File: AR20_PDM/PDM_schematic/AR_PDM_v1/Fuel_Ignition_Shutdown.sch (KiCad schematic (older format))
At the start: 21 parts

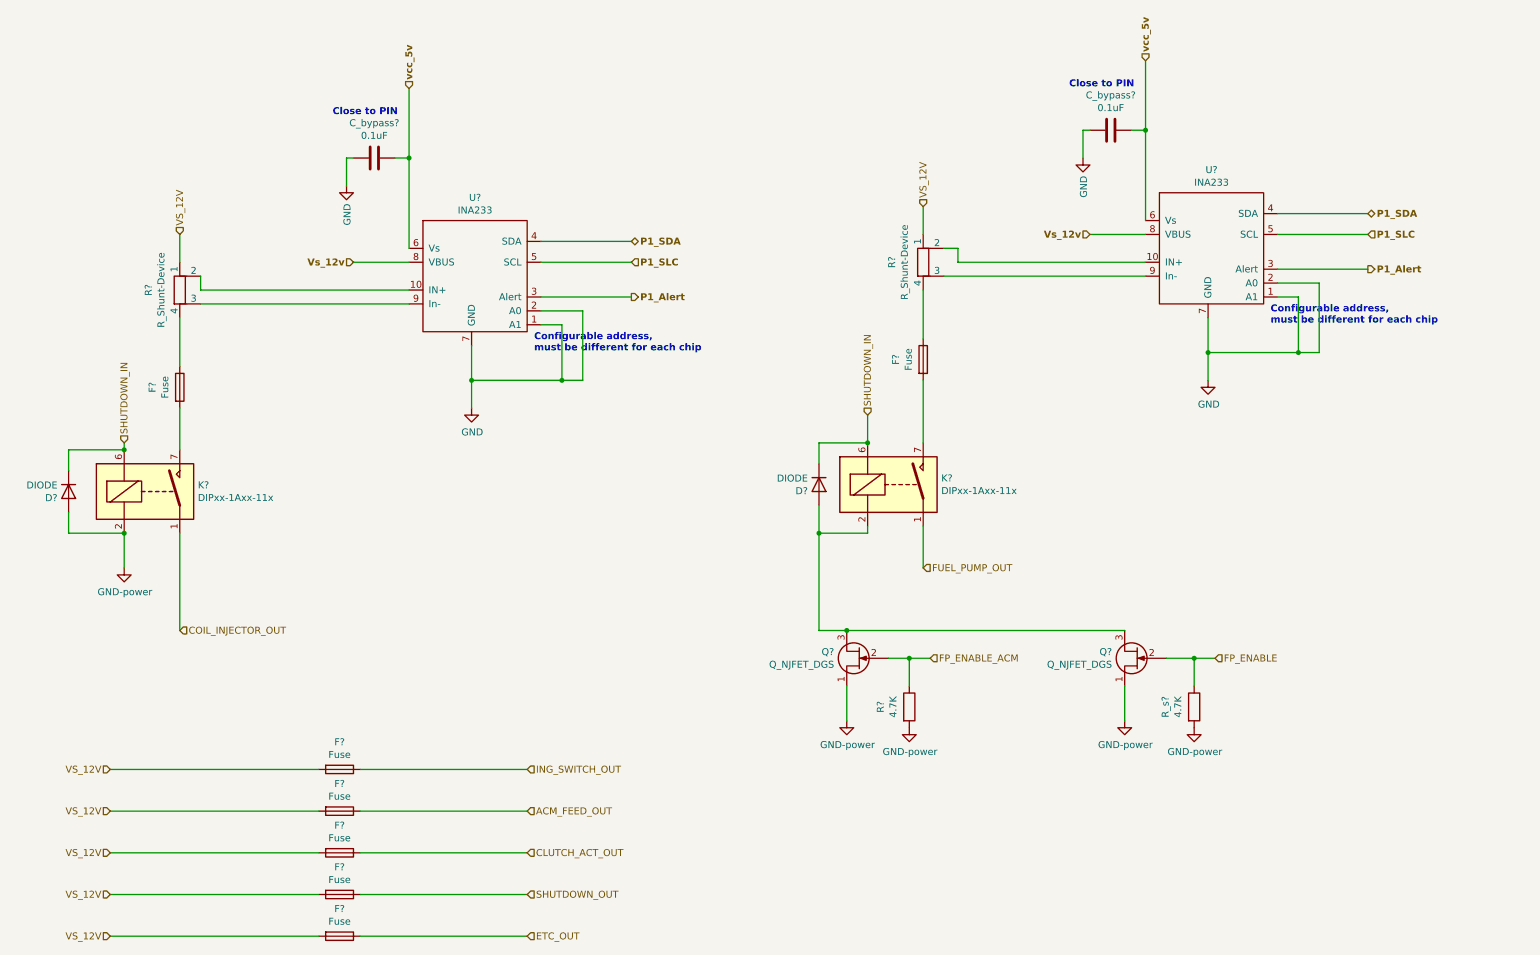
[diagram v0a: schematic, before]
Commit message: First draft of Gear phase, shutdown relays, and Direct phases.
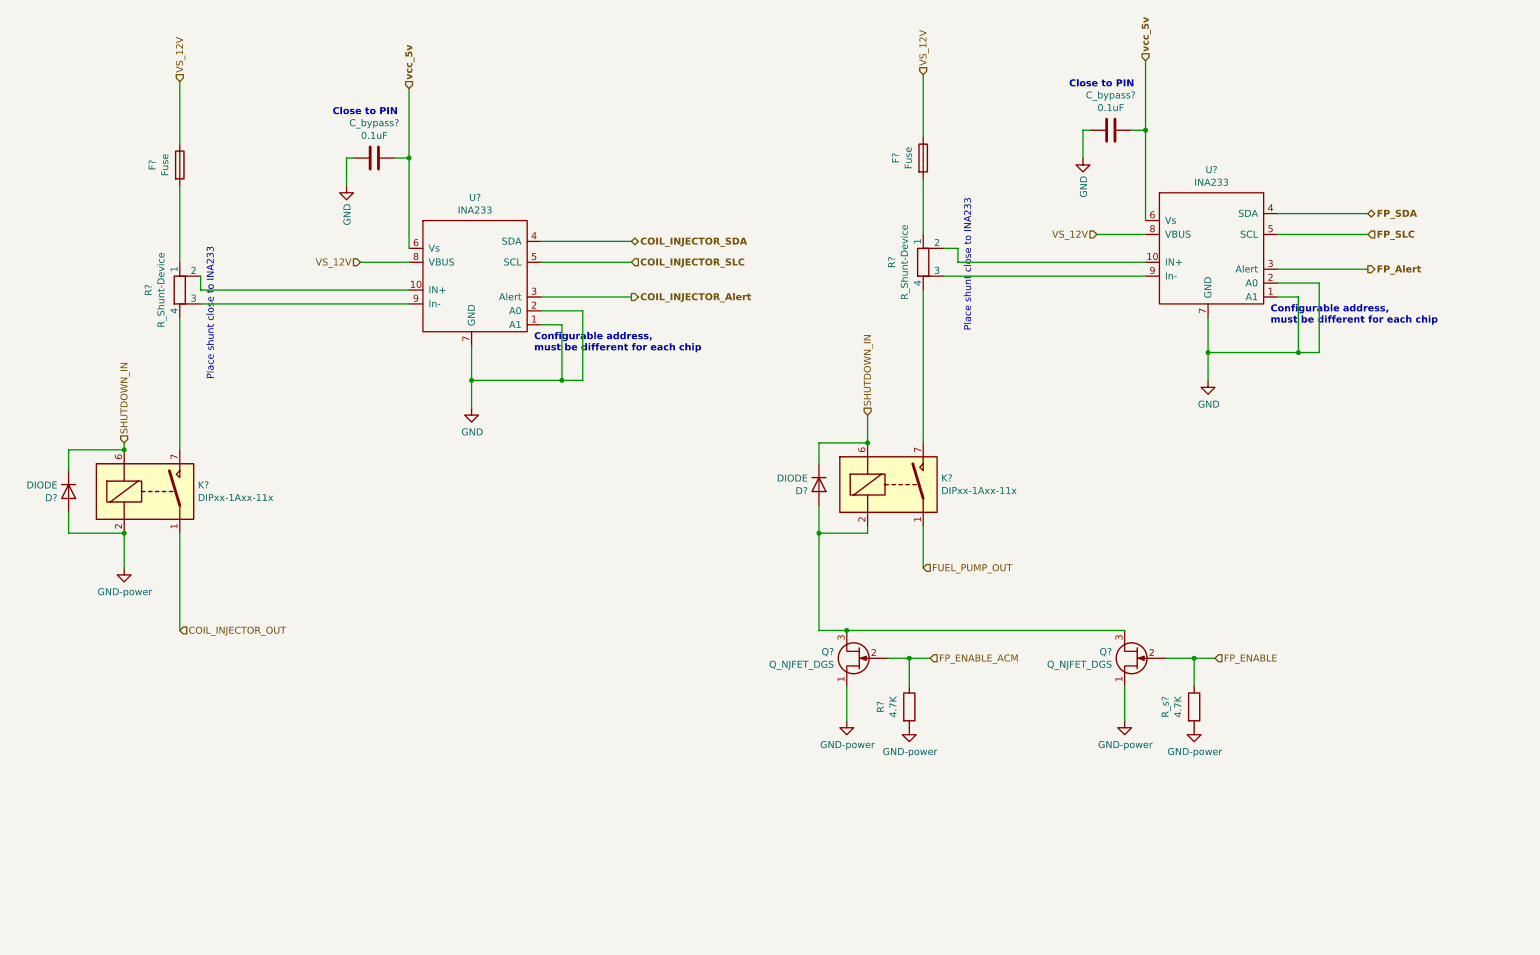
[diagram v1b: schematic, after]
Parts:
- removed F? (x6): Fuse, symbol Device:Fuse
- added F?: Fuse, symbol Device:Fuse
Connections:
- net Vs_12v is gone; now on net VS_12V: U?.8 (VBUS), U?.8 (VBUS)
- net VS_12V: now also F?.1, F?.1; no longer R?.1, R?.1
- net at R?.4: now also K?.7, K?.8
- net at K?.7, K?.8: now also R?.4; no longer F?.2
- net P1_Alert renamed COIL_INJECTOR_Alert
- net COIL_INJECTOR_Alert: no longer U?.3 (Alert)
- net P1_SDA renamed COIL_INJECTOR_SDA
- net COIL_INJECTOR_SDA: no longer U?.4 (SDA)
- net P1_SLC renamed COIL_INJECTOR_SLC
- net COIL_INJECTOR_SLC: no longer U?.5 (SCL)
- new net: F?.2, R?.1 (x2)
- new net FP_Alert: U?.3 (Alert)
- new net FP_SDA: U?.4 (SDA)
- new net FP_SLC: U?.5 (SCL)
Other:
- note added: "Place shunt close to INA233\n"
- moved on the sheet: F?
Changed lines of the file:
@@
 $Descr A4 11693 8268
 encoding utf-8
-Sheet 2 4
+Sheet 5 6
 Title ""
 Date ""
@@
 Comment4 ""
 $EndDescr
-$Comp
-L Device:Fuse F?
-U 1 1 5DDB2D60
-P 3150 6000
-F 0 "F?" V 2953 6000 50  0000 C CNN
-F 1 "Fuse" V 3044 6000 50  0000 C CNN
-F 2 "" V 3080 6000 50  0001 C CNN
-F 3 "~" H 3150 6000 50  0001 C CNN
-	1    3150 6000
-	0    1    1    0
-$EndComp
-Wire Wire Line
-	3000 6000 1500 6000
-Wire Wire Line
-	3300 6000 4500 6000
-Text HLabel 1500 6000 0    50   Input ~ 0
-VS_12V
-$Comp
-L Device:Fuse F?
-U 1 1 5DDB4A05
-P 3150 6300
-F 0 "F?" V 2953 6300 50  0000 C CNN
-F 1 "Fuse" V 3044 6300 50  0000 C CNN
-F 2 "" V 3080 6300 50  0001 C CNN
-F 3 "~" H 3150 6300 50  0001 C CNN
-	1    3150 6300
-	0    1    1    0
-$EndComp
-Wire Wire Line
-	3000 6300 1500 6300
-Wire Wire Line
-	3300 6300 4500 6300
-Text HLabel 1500 6300 0    50   Input ~ 0
-VS_12V
-$Comp
-L Device:Fuse F?
-U 1 1 5DDB4CFC
-P 3150 6600
-F 0 "F?" V 2953 6600 50  0000 C CNN
-F 1 "Fuse" V 3044 6600 50  0000 C CNN
-F 2 "" V 3080 6600 50  0001 C CNN
-F 3 "~" H 3150 6600 50  0001 C CNN
-	1    3150 6600
-	0    1    1    0
-$EndComp
-Wire Wire Line
-	3000 6600 1500 6600
-Wire Wire Line
-	3300 6600 4500 6600
-Text HLabel 1500 6600 0    50   Input ~ 0
-VS_12V
-$Comp
-L Device:Fuse F?
-U 1 1 5DDB67ED
-P 3150 6900
-F 0 "F?" V 2953 6900 50  0000 C CNN
-F 1 "Fuse" V 3044 6900 50  0000 C CNN
-F 2 "" V 3080 6900 50  0001 C CNN
-F 3 "~" H 3150 6900 50  0001 C CNN
-	1    3150 6900
-	0    1    1    0
-$EndComp
-Wire Wire Line
-	3000 6900 1500 6900
-Wire Wire Line
-	3300 6900 4500 6900
-Text HLabel 1500 6900 0    50   Input ~ 0
-VS_12V
-$Comp
-L Device:Fuse F?
-U 1 1 5DDB67F6
-P 3150 7200
-F 0 "F?" V 2953 7200 50  0000 C CNN
-F 1 "Fuse" V 3044 7200 50  0000 C CNN
-F 2 "" V 3080 7200 50  0001 C CNN
-F 3 "~" H 3150 7200 50  0001 C CNN
-	1    3150 7200
-	0    1    1    0
-$EndComp
-Wire Wire Line
-	3000 7200 1500 7200
-Wire Wire Line
-	3300 7200 4500 7200
-Text HLabel 1500 7200 0    50   Input ~ 0
-VS_12V
-Text HLabel 4500 6000 2    50   Input ~ 0
-ING_SWITCH_OUT
-Text HLabel 4500 6300 2    50   Input ~ 0
-ACM_FEED_OUT
-Text HLabel 4500 6600 2    50   Input ~ 0
-CLUTCH_ACT_OUT
-Text HLabel 4500 6900 2    50   Input ~ 0
-SHUTDOWN_OUT
-Text HLabel 4500 7200 2    50   Input ~ 0
-ETC_OUT
 Text HLabel 7350 4550 2    50   Input ~ 0
 FUEL_PUMP_OUT
@@
 	1    0    0    -1
 $EndComp
-Text HLabel 7350 1950 1    50   Input ~ 0
+Text HLabel 7350 1000 1    50   Input ~ 0
 VS_12V
 $Comp
 L Device:Fuse F?
 U 1 1 5DDF15AA
-P 7350 3050
-F 0 "F?" V 7153 3050 50  0000 C CNN
-F 1 "Fuse" V 7244 3050 50  0000 C CNN
-F 2 "" V 7280 3050 50  0001 C CNN
-F 3 "~" H 7350 3050 50  0001 C CNN
-	1    7350 3050
-	1    0    0    -1
-$EndComp
-Wire Wire Line
-	7350 1950 7350 2150
-Wire Wire Line
-	7350 2550 7350 2900
-Wire Wire Line
-	7350 3200 7350 3650
+P 7350 1600
+F 0 "F?" V 7153 1600 50  0000 C CNN
+F 1 "Fuse" V 7244 1600 50  0000 C CNN
+F 2 "" V 7280 1600 50  0001 C CNN
+F 3 "~" H 7350 1600 50  0001 C CNN
+	1    7350 1600
+	1    0    0    -1
+$EndComp
 $Comp
 L AR20_PDM_v1-rescue:C-Device C_bypass?
 U 1 1 5DE0EACB
 P 8700 1400
+AR Path="/5DA89415/5DE0EACB" Ref="C_bypass?"  Part="1"
+AR Path="/5DA8920B/5DE0EACB" Ref="C_bypass?"  Part="1"
 F 0 "C_bypass?" V 8448 1400 50  0000 C CNN
 F 1 "0.1uF" V 8539 1400 50  0000 C CNN
@@
 U 1 1 5DE0EAD1
 P 8500 1600
+AR Path="/5DA89415/5DE0EAD1" Ref="#PWR?"  Part="1"
+AR Path="/5DA8920B/5DE0EAD1" Ref="#PWR?"  Part="1"
 F 0 "#PWR?" H 8500 1350 50  0001 C CNN
 F 1 "GND" V 8505 1472 50  0000 R CNN
@@
 U 1 1 5DE0EAD8
 P 9400 3200
+AR Path="/5DA89415/5DE0EAD8" Ref="#PWR?"  Part="1"
+AR Path="/5DA8920B/5DE0EAD8" Ref="#PWR?"  Part="1"
 F 0 "#PWR?" H 9400 2950 50  0001 C CNN
 F 1 "GND" H 9405 3027 50  0000 C CNN
@@
 U 1 1 5DE0EAE7
 P 9400 2100
+AR Path="/5DA89415/5DE0EAE7" Ref="U?"  Part="1"
+AR Path="/5DA8920B/5DE0EAE7" Ref="U?"  Part="1"
 F 0 "U?" H 9425 2515 50  0000 C CNN
 F 1 "INA233" H 9425 2424 50  0000 C CNN
@@
 	1    0    0    -1
 $EndComp
-Text HLabel 8550 2150 0    50   Input ~ 10
-Vs_12v
 Text HLabel 8950 900  1    50   Input ~ 10
 vcc_5v
 Text HLabel 10550 2400 2    50   Output ~ 10
-P1_Alert
+FP_Alert
 Text HLabel 10550 2000 2    50   BiDi ~ 10
-P1_SDA
+FP_SDA
 Text HLabel 10550 2150 2    50   Input ~ 10
-P1_SLC
+FP_SLC
 Text Notes 8400 1100 0    50   ~ 10
 Close to PIN
-Wire Wire Line
-	8950 2150 8550 2150
 Wire Wire Line
 	9900 2150 10550 2150
@@
 Wire Wire Line
 	4600 2350 5250 2350
-Wire Wire Line
-	3650 2350 3250 2350
 Text Notes 3100 1300 0    50   ~ 10
 Close to PIN
 Text HLabel 5250 2350 2    50   Input ~ 10
-P1_SLC
+COIL_INJECTOR_SLC
 Text HLabel 5250 2200 2    50   BiDi ~ 10
-P1_SDA
+COIL_INJECTOR_SDA
 Text HLabel 5250 2600 2    50   Output ~ 10
-P1_Alert
+COIL_INJECTOR_Alert
 Text HLabel 3650 1100 1    50   Input ~ 10
 vcc_5v
-Text HLabel 3250 2350 0    50   Input ~ 10
-Vs_12v
 $Comp
 L AR20_PDM_v1-rescue:INA233 U?
 U 1 1 5DE077D0
 P 4100 2300
+AR Path="/5DA89415/5DE077D0" Ref="U?"  Part="1"
+AR Path="/5DA8920B/5DE077D0" Ref="U?"  Part="1"
 F 0 "U?" H 4125 2715 50  0000 C CNN
 F 1 "INA233" H 4125 2624 50  0000 C CNN
@@
 U 1 1 5DE077C1
 P 4100 3400
+AR Path="/5DA89415/5DE077C1" Ref="#PWR?"  Part="1"
+AR Path="/5DA8920B/5DE077C1" Ref="#PWR?"  Part="1"
 F 0 "#PWR?" H 4100 3150 50  0001 C CNN
 F 1 "GND" H 4105 3227 50  0000 C CNN
@@
 U 1 1 5DE077BA
 P 3200 1800
+AR Path="/5DA89415/5DE077BA" Ref="#PWR?"  Part="1"
+AR Path="/5DA8920B/5DE077BA" Ref="#PWR?"  Part="1"
 F 0 "#PWR?" H 3200 1550 50  0001 C CNN
 F 1 "GND" V 3205 1672 50  0000 R CNN
@@
 U 1 1 5DE077B4
 P 3400 1600
+AR Path="/5DA89415/5DE077B4" Ref="C_bypass?"  Part="1"
+AR Path="/5DA8920B/5DE077B4" Ref="C_bypass?"  Part="1"
 F 0 "C_bypass?" V 3148 1600 50  0000 C CNN
 F 1 "0.1uF" V 3239 1600 50  0000 C CNN
@@
 	0    1    1    0
 $EndComp
-Wire Wire Line
-	2000 2750 2000 3100
-Wire Wire Line
-	2000 2150 2000 2350
-$Comp
-L Device:Fuse F?
-U 1 1 5DDB7458
-P 2000 3250
-F 0 "F?" V 1803 3250 50  0000 C CNN
-F 1 "Fuse" V 1894 3250 50  0000 C CNN
-F 2 "" V 1930 3250 50  0001 C CNN
-F 3 "~" H 2000 3250 50  0001 C CNN
-	1    2000 3250
-	1    0    0    -1
-$EndComp
-Text HLabel 2000 2150 1    50   Input ~ 0
-VS_12V
 $Comp
 L Relay:DIPxx-1Axx-11x K?
@@
 Text HLabel 1600 3650 1    50   Input ~ 0
 SHUTDOWN_IN
-Wire Wire Line
-	2000 3400 2000 3700
 Wire Wire Line
 	1600 3700 1200 3700
@@
 	1    0    0    -1
 $EndComp
+Wire Wire Line
+	7350 1450 7350 1000
+Text HLabel 2000 1050 1    50   Input ~ 0
+VS_12V
+$Comp
+L Device:Fuse F?
+U 1 1 5DE5EBA7
+P 2000 1650
+F 0 "F?" V 1803 1650 50  0000 C CNN
+F 1 "Fuse" V 1894 1650 50  0000 C CNN
+F 2 "" V 1930 1650 50  0001 C CNN
+F 3 "~" H 2000 1650 50  0001 C CNN
+	1    2000 1650
+	1    0    0    -1
+$EndComp
+Wire Wire Line
+	2000 1500 2000 1050
+Wire Wire Line
+	2000 2750 2000 3700
+Wire Wire Line
+	7350 2550 7350 3650
+Text Notes 2250 3200 1    50   ~ 0
+Place shunt close to INA233\n
+Text Notes 7700 2850 1    50   ~ 0
+Place shunt close to INA233\n
+Wire Wire Line
+	2000 1800 2000 2350
+Text HLabel 3300 2350 0    50   Input ~ 0
+VS_12V
+Wire Wire Line
+	3650 2350 3300 2350
+Wire Wire Line
+	7350 1750 7350 2150
+Text HLabel 8600 2150 0    50   Input ~ 0
+VS_12V
+Wire Wire Line
+	8600 2150 8950 2150
 $EndSCHEMATC

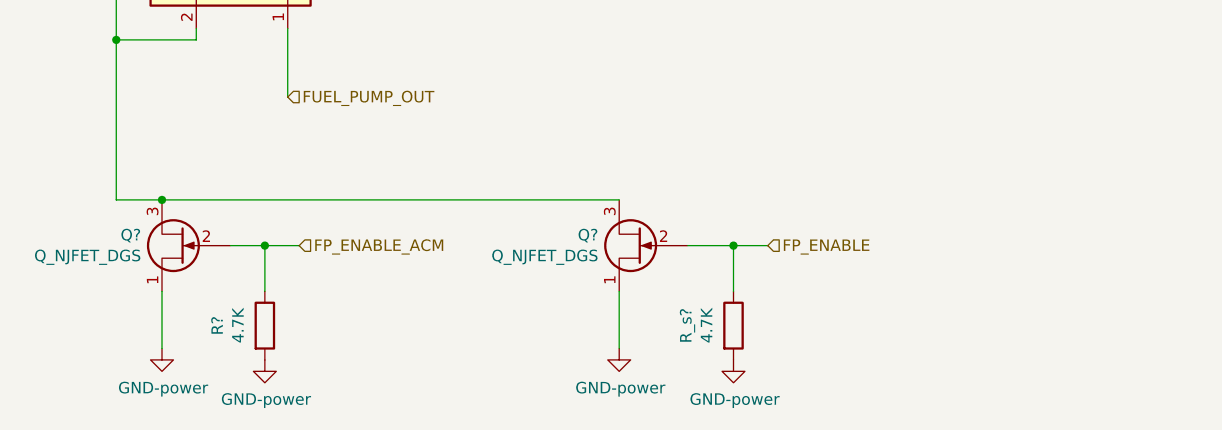
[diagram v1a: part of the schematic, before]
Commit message: Added label on mosfets, added fuel pump sinking output
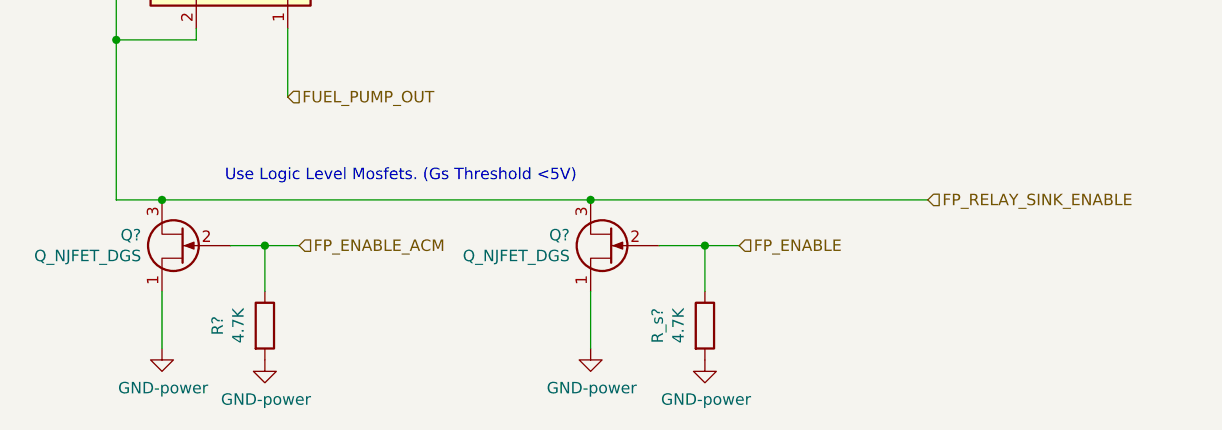
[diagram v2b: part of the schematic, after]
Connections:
- net FP_RELAY_SINK_ENABLE: now reaches D?.1 (A), K?.2, Q?.3 (S), Q?.3 (S)
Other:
- note added: "Use Logic Level Mosfets. (Gs Threshold <5V)"
- moved on the sheet: Q?, R_s?
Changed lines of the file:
@@
 $Descr A4 11693 8268
 encoding utf-8
-Sheet 5 6
+Sheet 4 6
 Title ""
 Date ""
@@
 L Device:Q_NJFET_DGS Q?
 U 1 1 5DDB5A55
-P 8900 5200
-F 0 "Q?" H 9091 5154 50  0000 L CNN
-F 1 "Q_NJFET_DGS" H 9091 5245 50  0000 L CNN
-F 2 "" H 9100 5300 50  0001 C CNN
-F 3 "~" H 8900 5200 50  0001 C CNN
-	1    8900 5200
+P 8775 5200
+F 0 "Q?" H 8966 5154 50  0000 L CNN
+F 1 "Q_NJFET_DGS" H 8966 5245 50  0000 L CNN
+F 2 "" H 8975 5300 50  0001 C CNN
+F 3 "~" H 8775 5200 50  0001 C CNN
+	1    8775 5200
 	-1   0    0    1
 $EndComp
@@
 L AR20_PDM_v1-rescue:R-Device R_s?
 U 1 1 5DDB5A5B
-P 9300 5550
+P 9175 5550
 AR Path="/5DA89415/5DDB5A5B" Ref="R_s?"  Part="1"
 AR Path="/5DA8920B/5DDB5A5B" Ref="R?"  Part="1"
-F 0 "R?" V 9093 5550 50  0000 C CNN
-F 1 "4.7K" V 9184 5550 50  0000 C CNN
-F 2 "" V 9230 5550 50  0001 C CNN
-F 3 "~" H 9300 5550 50  0001 C CNN
-	1    9300 5550
+F 0 "R?" V 8968 5550 50  0000 C CNN
+F 1 "4.7K" V 9059 5550 50  0000 C CNN
+F 2 "" V 9105 5550 50  0001 C CNN
+F 3 "~" H 9175 5550 50  0001 C CNN
+	1    9175 5550
 	1    0    0    -1
 $EndComp
@@
 L AR20_PDM_v1-rescue:GND-power #PWR?
 U 1 1 5DDB5A61
-P 9300 5700
-F 0 "#PWR?" H 9300 5450 50  0001 C CNN
-F 1 "GND-power" H 9305 5527 50  0000 C CNN
-F 2 "" H 9300 5700 50  0001 C CNN
-F 3 "" H 9300 5700 50  0001 C CNN
-	1    9300 5700
-	1    0    0    -1
-$EndComp
-Wire Wire Line
-	9100 5200 9300 5200
+P 9175 5700
+F 0 "#PWR?" H 9175 5450 50  0001 C CNN
+F 1 "GND-power" H 9180 5527 50  0000 C CNN
+F 2 "" H 9175 5700 50  0001 C CNN
+F 3 "" H 9175 5700 50  0001 C CNN
+	1    9175 5700
+	1    0    0    -1
+$EndComp
 $Comp
 L AR20_PDM_v1-rescue:GND-power #PWR?
 U 1 1 5DDB5A6B
-P 8800 5650
-F 0 "#PWR?" H 8800 5400 50  0001 C CNN
-F 1 "GND-power" H 8805 5477 50  0000 C CNN
-F 2 "" H 8800 5650 50  0001 C CNN
-F 3 "" H 8800 5650 50  0001 C CNN
-	1    8800 5650
-	1    0    0    -1
-$EndComp
-Wire Wire Line
-	8800 5400 8800 5650
-Wire Wire Line
-	6800 5000 8800 5000
+P 8675 5650
+F 0 "#PWR?" H 8675 5400 50  0001 C CNN
+F 1 "GND-power" H 8680 5477 50  0000 C CNN
+F 2 "" H 8675 5650 50  0001 C CNN
+F 3 "" H 8675 5650 50  0001 C CNN
+	1    8675 5650
+	1    0    0    -1
+$EndComp
+Wire Wire Line
+	8675 5400 8675 5650
+Wire Wire Line
+	6800 5000 8675 5000
 Connection ~ 6800 5000
-Text HLabel 9450 5200 2    50   Input ~ 0
-FP_ENABLE
-Wire Wire Line
-	9300 5400 9300 5200
-Connection ~ 9300 5200
-Wire Wire Line
-	9300 5200 9450 5200
 $Comp
 L AR20_PDM_v1-rescue:R-Device R?
@@
 Wire Wire Line
 	8600 2150 8950 2150
+Text HLabel 9325 5200 2    50   Input ~ 0
+FP_ENABLE
+Wire Wire Line
+	8975 5200 9175 5200
+Wire Wire Line
+	9175 5200 9175 5400
+Wire Wire Line
+	9325 5200 9175 5200
+Connection ~ 9175 5200
+Connection ~ 8675 5000
+Text HLabel 10150 5000 2    50   Input ~ 0
+FP_RELAY_SINK_ENABLE
+Wire Wire Line
+	8675 5000 10150 5000
+Text Notes 7075 4925 0    50   ~ 0
+Use Logic Level Mosfets. (Gs Threshold <5V)
 $EndSCHEMATC
